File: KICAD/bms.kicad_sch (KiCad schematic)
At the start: 25 parts, among them J801 DC_Jack_ALIM, J802 NiMH_Conn, J803 Li-Ion_Conn, Q801 NMOS, Q802 NMOS, Q803 PMOS, U801 LTC1731ES8-8_4

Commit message: update schematics
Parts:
- C801: value 0.1µ -> 0.1µF; footprint (none) -> Capacitor_SMD:C_0603_1608Metric
- C802, C803, C805: footprint (none) -> Capacitor_SMD:C_0603_1608Metric
- C804: value 100n -> 100nF; footprint (none) -> Capacitor_SMD:C_0603_1608Metric
- C806: value 1µ -> 1µF; footprint (none) -> Capacitor_SMD:C_0603_1608Metric
- D801: footprint (none) -> LED_SMD:LED_0603_1608Metric
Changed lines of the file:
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@@
     (stroke (width 0) (type default))
   )
-  (wire (pts (xy 124.46 97.79) (xy 135.89 97.79))
+  (wire (pts (xy 124.46 97.79) (xy 137.16 97.79))
     (stroke (width 0) (type default))
   )
@@
     (stroke (width 0) (type default))
   )
-  (wire (pts (xy 132.08 118.11) (xy 134.62 118.11))
+  (wire (pts (xy 132.08 118.11) (xy 137.16 118.11))
     (stroke (width 0) (type default))
   )
@@
     )
   )
-  (global_label "Li_Ion+" (shape input) (at 135.89 97.79 0) (fields_autoplaced)
-    (effects (font (size 1.27 1.27)) (justify left))
-    (property "Intersheetrefs" "${INTERSHEET_REFS}" (at 145.9509 97.79 0)
+  (global_label "Li_Ion+" (shape input) (at 137.16 97.79 0) (fields_autoplaced)
+    (effects (font (size 1.27 1.27)) (justify left))
+    (property "Intersheetrefs" "${INTERSHEET_REFS}" (at 147.2209 97.79 0)
       (effects (font (size 1.27 1.27)) (justify left) hide)
     )
@@
     )
   )
-  (global_label "Li_Ion-" (shape input) (at 134.62 118.11 0) (fields_autoplaced)
-    (effects (font (size 1.27 1.27)) (justify left))
-    (property "Intersheetrefs" "${INTERSHEET_REFS}" (at 144.6809 118.11 0)
+  (global_label "Li_Ion-" (shape input) (at 137.16 118.11 0) (fields_autoplaced)
+    (effects (font (size 1.27 1.27)) (justify left))
+    (property "Intersheetrefs" "${INTERSHEET_REFS}" (at 147.2209 118.11 0)
       (effects (font (size 1.27 1.27)) (justify left) hide)
     )
@@
       (effects (font (size 1.27 1.27)) (justify left))
     )
-    (property "Value" "0.1µ" (at 81.28 73.6663 0)
-      (effects (font (size 1.27 1.27)) (justify left))
-    )
-    (property "Footprint" "" (at 78.74 72.39 0)
+    (property "Value" "0.1µF" (at 81.28 73.6663 0)
+      (effects (font (size 1.27 1.27)) (justify left))
+    )
+    (property "Footprint" "Capacitor_SMD:C_0603_1608Metric" (at 78.74 72.39 0)
       (effects (font (size 1.27 1.27)) hide)
     )
@@
       (effects (font (size 1.27 1.27)) (justify left))
     )
-    (property "Footprint" "" (at 157.48 74.93 0)
+    (property "Footprint" "Capacitor_SMD:C_0603_1608Metric" (at 157.48 74.93 0)
       (effects (font (size 1.27 1.27)) hide)
     )
@@
       (effects (font (size 1.27 1.27)) (justify left))
     )
-    (property "Value" "100n" (at 134.62 114.3063 0)
-      (effects (font (size 1.27 1.27)) (justify left))
-    )
-    (property "Footprint" "" (at 132.08 113.03 0)
+    (property "Value" "100nF" (at 134.62 114.3063 0)
+      (effects (font (size 1.27 1.27)) (justify left))
+    )
+    (property "Footprint" "Capacitor_SMD:C_0603_1608Metric" (at 132.08 113.03 0)
       (effects (font (size 1.27 1.27)) hide)
     )
@@
       (effects (font (size 1.27 1.27)) (justify left))
     )
-    (property "Footprint" "" (at 91.44 113.03 0)
+    (property "Footprint" "Capacitor_SMD:C_0603_1608Metric" (at 91.44 113.03 0)
       (effects (font (size 1.27 1.27)) hide)
     )
@@
       (effects (font (size 1.27 1.27)) (justify right))
     )
-    (property "Footprint" "" (at 78.74 57.15 0)
+    (property "Footprint" "LED_SMD:LED_0603_1608Metric" (at 78.74 57.15 0)
       (effects (font (size 1.27 1.27)) hide)
     )
@@
       (effects (font (size 1.27 1.27)) (justify left))
     )
-    (property "Value" "1µ" (at 175.26 54.6163 0)
-      (effects (font (size 1.27 1.27)) (justify left))
-    )
-    (property "Footprint" "" (at 172.72 53.34 0)
+    (property "Value" "1µF" (at 175.26 54.6163 0)
+      (effects (font (size 1.27 1.27)) (justify left))
+    )
+    (property "Footprint" "Capacitor_SMD:C_0603_1608Metric" (at 172.72 53.34 0)
       (effects (font (size 1.27 1.27)) hide)
     )
@@
       (effects (font (size 1.27 1.27)) (justify left))
     )
-    (property "Footprint" "" (at 91.44 120.65 0)
-      (effects (font (size 1.27 1.27)) hide)
-    )
+    (property "Footprint" "Capacitor_SMD:C_0603_1608Metric" (at 91.44 120.65 0)
+      (effects (font (size 1.27 1.27)) hide)
+    )

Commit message: Completed schematics
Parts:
- C805: footprint Capacitor_SMD:C_0603_1608Metric -> Capacitor_SMD:CP_Elec_5x5.4
- D802: footprint (none) -> Diode_SMD:D_SMA
- F801: footprint (none) -> Fuse:Fuse_1206_3216Metric
- J801: footprint (none) -> DCJack_footprint:WE_694102303002
- J802: footprint (none) -> Connector_JST:JST_XH_S2B-XH-A_1x02_P2.50mm_Horizontal
- J803: footprint (none) -> Connector_JST:JST_XH_S3B-XH-A_1x03_P2.50mm_Horizontal
- JP801: value SolderJumper_3_Open -> SolderJumper; footprint (none) -> Jumper:SolderJumper-3_P2.0mm_Open_TrianglePad1.0x1.5mm
- Q801, Q802, Q803: footprint (none) -> Package_TO_SOT_SMD:SOT-23
- R801, R802, R803, R804, R805, R806: footprint (none) -> Resistor_SMD:R_0603_1608Metric
- R_SENSE801: footprint (none) -> Resistor_SMD:R_1206_3216Metric
- U801: footprint LTC1731ES8-8_4:SO-8_S -> Package_SO:SO-8_3.9x4.9mm_P1.27mm
- U802: footprint (none) -> Package_SO:MSOP-8_3x3mm_P0.65mm
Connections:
- net BAT+: now also F801.1; no longer JP801.2 (C)
- net NiMh+: now also JP801.3 (B); no longer F801.2
- new net: F801.2, JP801.2 (C)
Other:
- note added: "Empreinte en 1206 car la résistance de shunt dissipe beaucoup de puissance"
- note added: "Protection de retour de courant sur chargeur"
- moved on the sheet: F801, JP801

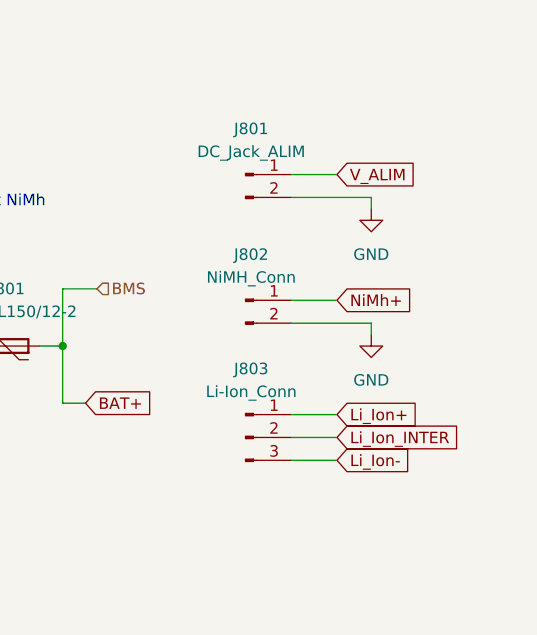
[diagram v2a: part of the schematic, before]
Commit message: update polarity connectors
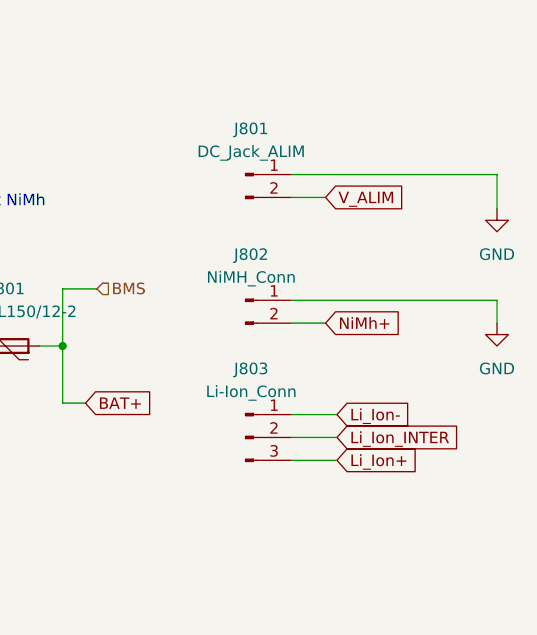
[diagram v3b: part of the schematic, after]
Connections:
- net GND: now also J801.1 (Pin_1), J802.1 (Pin_1); no longer J801.2 (Pin_2), J802.2 (Pin_2)
- net Li_Ion+: now also J803.3 (Pin_3); no longer J803.1 (Pin_1)
- net Li_Ion-: now also J803.1 (Pin_1); no longer J803.3 (Pin_3)
- net NiMh+: now also J802.2 (Pin_2); no longer J802.1 (Pin_1)
- net V_ALIM: now also J801.2 (Pin_2); no longer J801.1 (Pin_1)

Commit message: PCB finalized
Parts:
- removed J801: DC_Jack_ALIM, DCJack_footprint:WE_694102303002, symbol Connector:Conn_01x02_Pin
- added J801: 694102303002, Connector_BarrelJack:BarrelJack_Wuerth_6941xx301002, symbol DC_JACK:694102303002
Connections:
- net GND: now also J801.2, J801.3
- net V_ALIM: now also J801.1
- net Secu_Vc: now reaches C802.2, C803.1, R803.1, U802.6 (Vc)
- net Secu_Dout: now reaches Q801.2 (G), U802.8 (Dout)
- net Secu_Sense: now reaches C804.1, R804.2, U802.5 (Sense)
- net Secu_VDD: now reaches C802.1, R802.1, U802.1 (VDD)
- net Secu_Vout: now reaches Q802.2 (G), U802.2 (Cout)
- net Secu_V-: now reaches R805.1, U802.3 (V-)
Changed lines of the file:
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@@
   (junction (at 91.44 116.84) (diameter 0) (color 0 0 0 0)
+  )
+  (junction (at 219.71 88.9) (diameter 0) (color 0 0 0 0)
   )
   (no_connect (at 121.92 123.19))
@@
     (stroke (width 0) (type default))
   )
-  (wire (pts (xy 241.3 88.9) (xy 241.3 92.71))
+  (wire (pts (xy 236.22 88.9) (xy 236.22 92.71))
     (stroke (width 0) (type default))
   )
@@
     (stroke (width 0) (type default))
   )
-  (wire (pts (xy 218.44 88.9) (xy 241.3 88.9))
+  (wire (pts (xy 219.71 88.9) (xy 236.22 88.9))
     (stroke (width 0) (type default))
   )
@@
     (stroke (width 0) (type default))
   )
+  (wire (pts (xy 219.71 86.36) (xy 219.71 88.9))
+    (stroke (width 0) (type default))
+  )
   (wire (pts (xy 99.06 106.68) (xy 91.44 106.68))
     (stroke (width 0) (type default))
@@
     (stroke (width 0) (type default))
   )
-  (wire (pts (xy 218.44 91.44) (xy 222.25 91.44))
-    (stroke (width 0) (type default))
-  )
   (wire (pts (xy 133.35 64.77) (xy 149.86 64.77))
     (stroke (width 0) (type default))
@@
   )
   (wire (pts (xy 181.61 107.95) (xy 182.88 107.95))
+    (stroke (width 0) (type default))
+  )
+  (wire (pts (xy 219.71 83.82) (xy 224.79 83.82))
     (stroke (width 0) (type default))
   )
@@
   )
   (text "Charge Batterie" (at 102.87 39.37 0)
+    (effects (font (size 1.27 1.27)) (justify left bottom))
+  )
+  (label "Secu_Vc" (at 95.25 116.84 0) (fields_autoplaced)
+    (effects (font (size 1.27 1.27)) (justify left bottom))
+  )
+  (label "Secu_VSS" (at 95.25 127 0) (fields_autoplaced)
+    (effects (font (size 1.27 1.27)) (justify left bottom))
+  )
+  (label "Secu_V-" (at 125.73 116.84 0) (fields_autoplaced)
+    (effects (font (size 1.27 1.27)) (justify left bottom))
+  )
+  (label "Secu_Sense" (at 128.27 110.49 0) (fields_autoplaced)
+    (effects (font (size 1.27 1.27)) (justify left bottom))
+  )
+  (label "Secu_VDD" (at 95.25 106.68 0) (fields_autoplaced)
+    (effects (font (size 1.27 1.27)) (justify left bottom))
+  )
+  (label "Secu_Dout" (at 107.95 129.54 0) (fields_autoplaced)
+    (effects (font (size 1.27 1.27)) (justify left bottom))
+  )
+  (label "Secu_Vout" (at 119.38 129.54 0) (fields_autoplaced)
     (effects (font (size 1.27 1.27)) (justify left bottom))
   )
@@
     )
   )
-  (global_label "V_ALIM" (shape input) (at 222.25 91.44 0) (fields_autoplaced)
-    (effects (font (size 1.27 1.27)) (justify left))
-    (property "Intersheetrefs" "${INTERSHEET_REFS}" (at 231.4643 91.44 0)
+  (global_label "V_ALIM" (shape input) (at 224.79 83.82 0) (fields_autoplaced)
+    (effects (font (size 1.27 1.27)) (justify left))
+    (property "Intersheetrefs" "${INTERSHEET_REFS}" (at 234.0043 83.82 0)
       (effects (font (size 1.27 1.27)) (justify left) hide)
     )
@@
     )
   )
-  (symbol (lib_id "power:GND") (at 241.3 92.71 0) (unit 1)
-    (in_bom yes) (on_board yes) (dnp no) (fields_autoplaced)
-    (property "Reference" "#PWR0803" (at 241.3 99.06 0)
-      (effects (font (size 1.27 1.27)) hide)
-    )
-    (property "Value" "GND" (at 241.3 97.79 0)
-      (effects (font (size 1.27 1.27)))
-    )
-    (property "Footprint" "" (at 241.3 92.71 0)
-      (effects (font (size 1.27 1.27)) hide)
-    )
-    (property "Datasheet" "" (at 241.3 92.71 0)
+  (symbol (lib_id "power:GND") (at 236.22 92.71 0) (unit 1)
+    (in_bom yes) (on_board yes) (dnp no) (fields_autoplaced)
+    (property "Reference" "#PWR0803" (at 236.22 99.06 0)
+      (effects (font (size 1.27 1.27)) hide)
+    )
+    (property "Value" "GND" (at 236.22 97.79 0)
+      (effects (font (size 1.27 1.27)))
+    )
+    (property "Footprint" "" (at 236.22 92.71 0)
+      (effects (font (size 1.27 1.27)) hide)
+    )
+    (property "Datasheet" "" (at 236.22 92.71 0)
       (effects (font (size 1.27 1.27)) hide)
     )
@@
     )
   )
+  (symbol (lib_id "DC_JACK:694102303002") (at 214.63 86.36 0) (unit 1)
+    (in_bom yes) (on_board yes) (dnp no) (fields_autoplaced)
+    (property "Reference" "J801" (at 213.6775 77.47 0)
+      (effects (font (size 1.27 1.27)))
+    )
+    (property "Value" "694102303002" (at 213.6775 80.01 0)
+      (effects (font (size 1.27 1.27)))
+    )
+    (property "Footprint" "Connector_BarrelJack:BarrelJack_Wuerth_6941xx301002" (at 214.63 86.36 0)
+      (effects (font (size 1.27 1.27)) (justify bottom) hide)
+    )
+    (property "Datasheet" "" (at 214.63 86.36 0)
+      (effects (font (size 1.27 1.27)) hide)
+    )
+    (property "MF" "Wurth Electronics" (at 214.63 86.36 0)
+      (effects (font (size 1.27 1.27)) (justify bottom) hide)
+    )
+    (property "MAXIMUM_PACKAGE_HEIGHT" "7.60 mm" (at 214.63 86.36 0)
+      (effects (font (size 1.27 1.27)) (justify bottom) hide)
+    )
+    (property "Package" "None" (at 214.63 86.36 0)
+      (effects (font (size 1.27 1.27)) (justify bottom) hide)
+    )
+    (property "Price" "None" (at 214.63 86.36 0)
+      (effects (font (size 1.27 1.27)) (justify bottom) hide)
+    )
+    (property "Check_prices" "https://www.snapeda.com/parts/694102303002/Wurth+Electronics+Inc./view-part/?ref=eda" (at 214.63 86.36 0)
+      (effects (font (size 1.27 1.27)) (justify bottom) hide)
+    )
+    (property "STANDARD" "Manufacturer Recommendation" (at 214.63 86.36 0)
+      (effects (font (size 1.27 1.27)) (justify bottom) hide)
+    )
+    (property "PARTREV" "A" (at 214.63 86.36 0)
+      (effects (font (size 1.27 1.27)) (justify bottom) hide)
+    )
+    (property "SnapEDA_Link" "https://www.snapeda.com/parts/694102303002/Wurth+Electronics+Inc./view-part/?ref=snap" (at 214.63 86.36 0)
+      (effects (font (size 1.27 1.27)) (justify bottom) hide)
+    )
+    (property "MP" "694102303002" (at 214.63 86.36 0)
+      (effects (font (size 1.27 1.27)) (justify bottom) hide)
+    )
+    (property "Description" "\nPower Barrel Connector Jack 1.05mm ID (0.041), 3.50mm OD (0.138) Through Hole, Right Angle\n" (at 214.63 86.36 0)
+      (effects (font (size 1.27 1.27)) (justify bottom) hide)
+    )
+    (property "Availability" "In Stock" (at 214.63 86.36 0)
+      (effects (font (size 1.27 1.27)) (justify bottom) hide)
+    )
+    (property "MANUFACTURER" "Wurth Elektronik" (at 214.63 86.36 0)
+      (effects (font (size 1.27 1.27)) (justify bottom) hide)
+    )
+    (pin "1")
+    (pin "2")
+    (pin "3")
+    (instances
+      (project "kicad_chat-souris"
+        (path "/b1ddc66d-dbe7-4cff-b97f-1f0ce7ceeee4/6a44a42c-5fbe-4248-b986-7ff99c499b51/f1128ad6-8756-437f-94b0-49954c552a55"
+          (reference "J801") (unit 1)
+        )
+      )
+    )
+  )
   (symbol (lib_id "power:GND") (at 99.06 80.01 0) (unit 1)
     (in_bom yes) (on_board yes) (dnp no) (fields_autoplaced)
@@
         )
       )
-    )
-  )
-  (symbol (lib_id "Connector:Conn_01x02_Pin") (at 213.36 88.9 0) (unit 1)
-    (in_bom yes) (on_board yes) (dnp no) (fields_autoplaced)
-    (property "Reference" "J801" (at 213.995 83.82 0)
-      (effects (font (size 1.27 1.27)))
-    )
-    (property "Value" "DC_Jack_ALIM" (at 213.995 86.36 0)
-      (effects (font (size 1.27 1.27)))
-    )
-    (property "Footprint" "DCJack_footprint:WE_694102303002" (at 213.36 88.9 0)
-      (effects (font (size 1.27 1.27)) hide)
-    )
-    (property "Datasheet" "~" (at 213.36 88.9 0)
-      (effects (font (size 1.27 1.27)) hide)
-    )
-    (pin "1")
-    (pin "2")
-    (instances
-      (project "kicad_chat-souris"
-        (path "/b1ddc66d-dbe7-4cff-b97f-1f0ce7ceeee4/6a44a42c-5fbe-4248-b986-7ff99c499b51/f1128ad6-8756-437f-94b0-49954c552a55"
-          (reference "J801") (unit 1)
-        )
-      )
-      (project "PCB_Projet_Chat"
-        (path "/cdbf4f77-03ab-46d2-bfa4-0d7964539941"
-          (reference "J3") (unit 1)
-        )
-        (path "/cdbf4f77-03ab-46d2-bfa4-0d7964539941/15be8cd5-33ca-4f31-987a-0e88607c342b"
-          (reference "J201") (unit 1)
-        )
-      )
